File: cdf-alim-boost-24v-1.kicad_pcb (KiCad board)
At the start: 4 copper layers, 89 parts, among them J1 Conn_01x02, J2 Conn_01x02, J3 Conn_01x02, Q1 BSC019N04LS, Q2 BSC019N04LS, Q3 BSC019N04LS, Q4 BSC019N04LS, Q5 BSC019N04LS, U1 HT753-1, U2 TPS25983, U4 LM5122

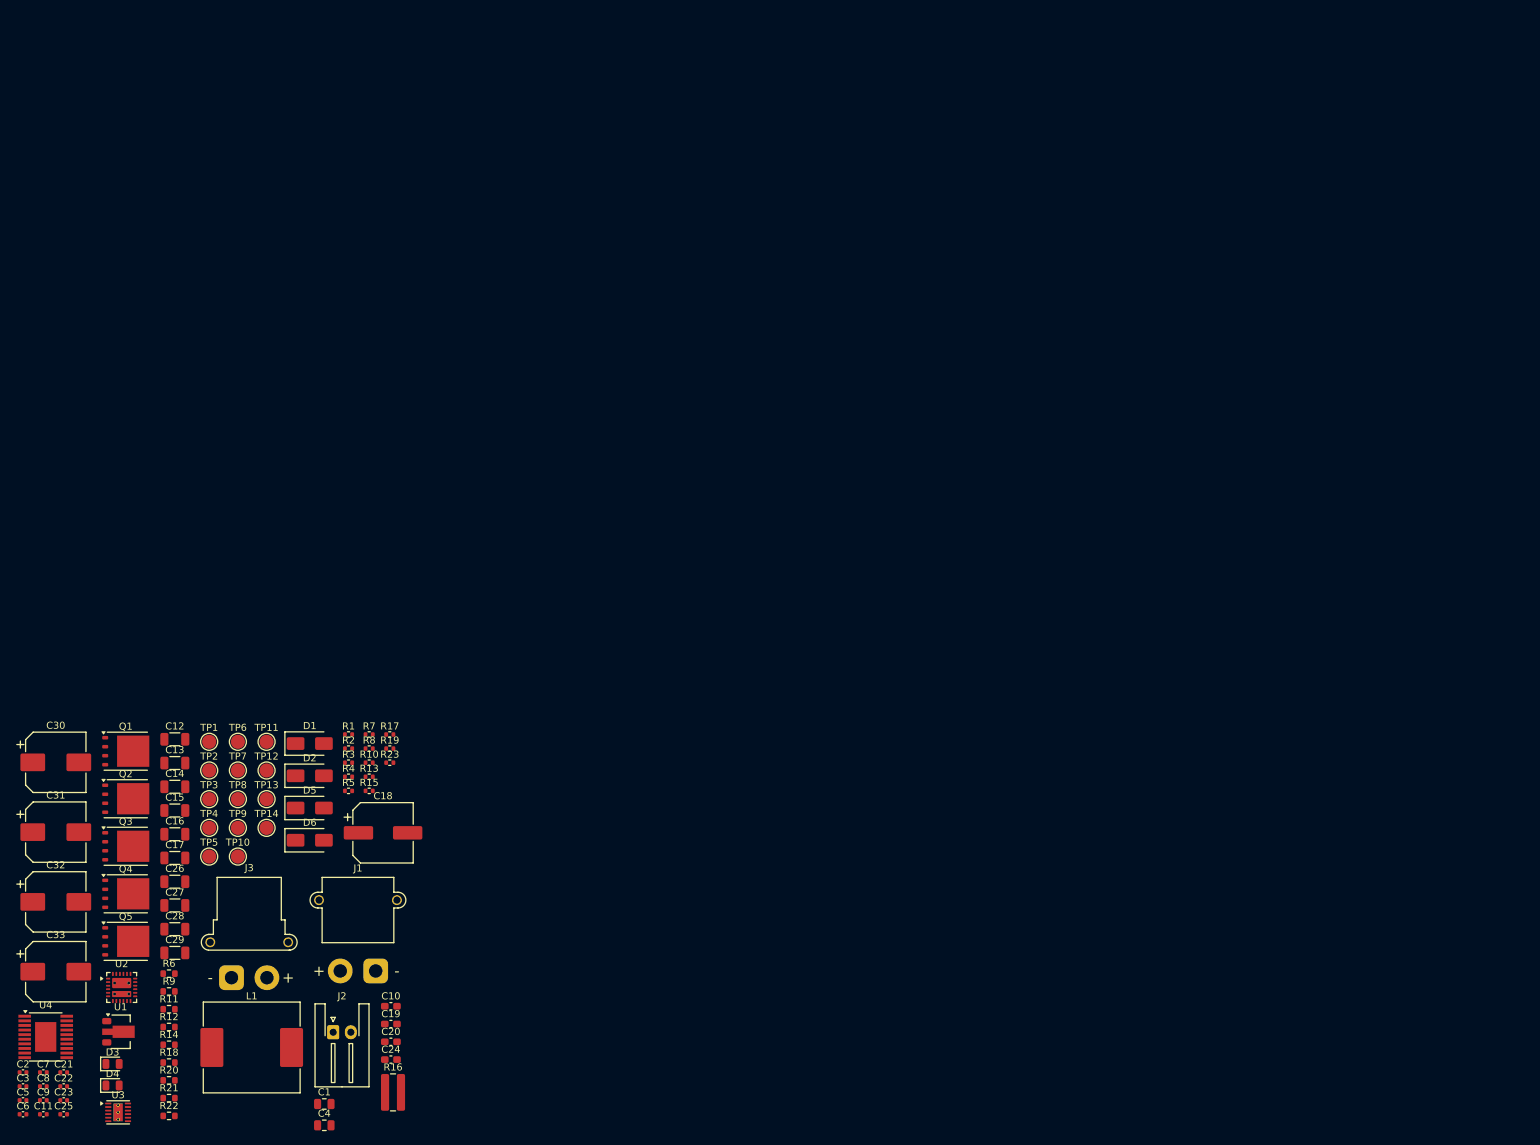
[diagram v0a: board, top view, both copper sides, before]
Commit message: pcb: initial sectionning
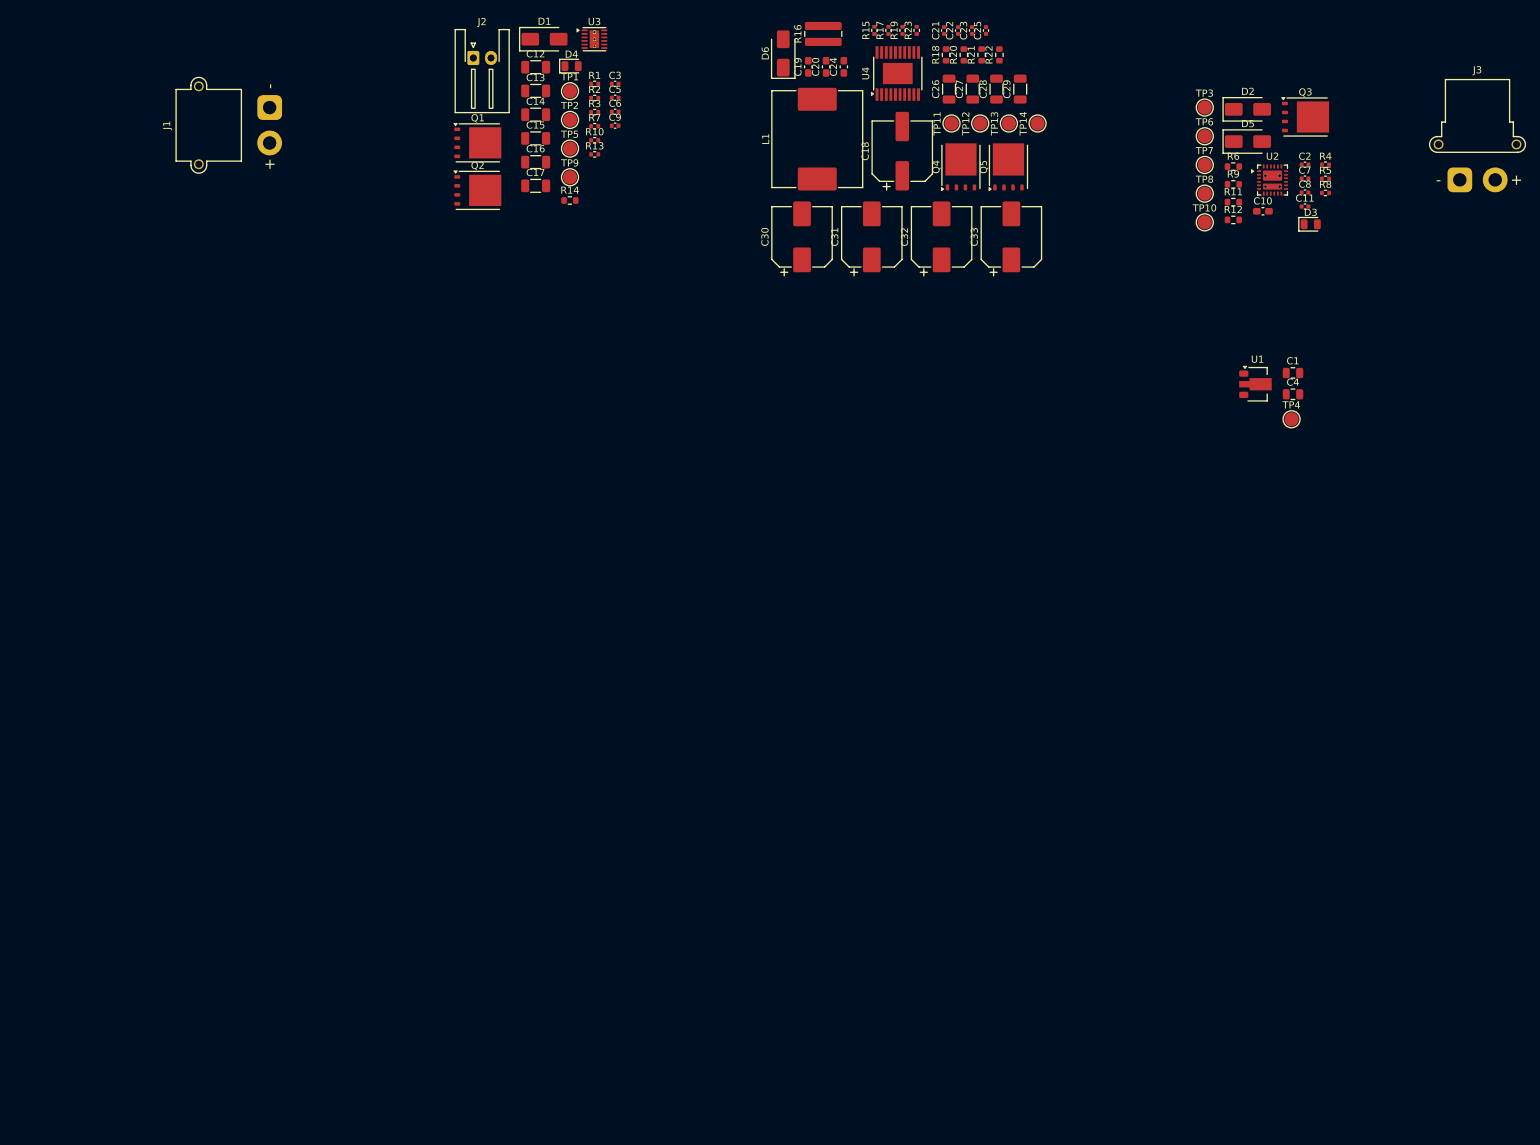
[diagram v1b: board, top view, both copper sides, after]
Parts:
- moved C2 221.7 mm to (199.2, 58.3)
- moved C11 219.4 mm to (199.2, 64.2)
- moved C7 218.3 mm to (199.2, 60.3)
- moved C8 218.3 mm to (199.2, 62.2)
- moved J3 206.8 mm to (221.0, 60.5)
- moved D3 206.5 mm to (200.0, 66.7)
- moved C25 200.9 mm to (154.1, 39.4), turned to 90 degrees
- moved U2 198.4 mm to (194.6, 60.5)
- moved C23 198.1 mm to (152.2, 39.4), turned to 90 degrees
- moved Q3 195.8 mm to (199.2, 51.6)
- moved C22 195.3 mm to (150.2, 39.4), turned to 90 degrees
- moved C21 192.6 mm to (148.2, 39.4), turned to 90 degrees
- moved R22 190.2 mm to (156.0, 42.8), turned to 90 degrees
- moved R11 188.5 mm to (189.0, 63.6)
- moved R12 188.5 mm to (189.0, 66.1)
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
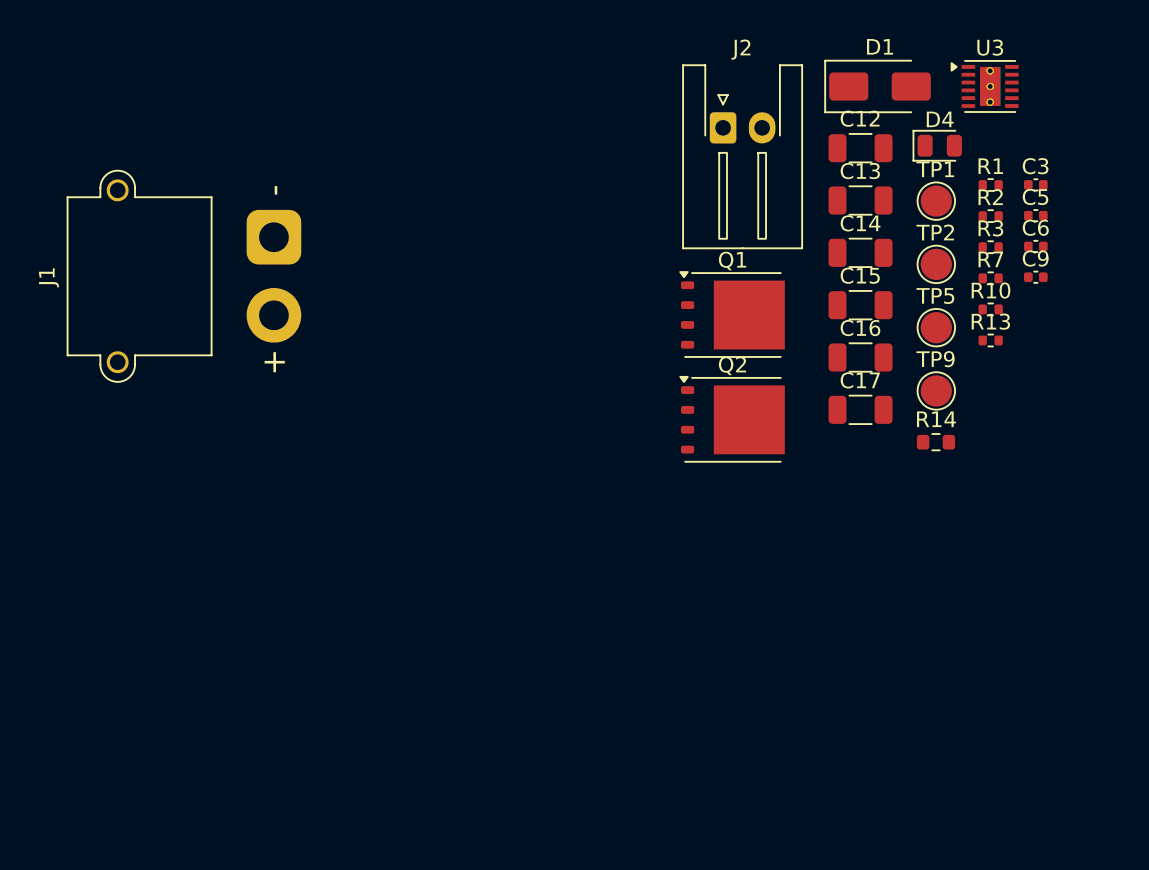
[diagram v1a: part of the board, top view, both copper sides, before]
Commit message: pcb: add lm7480 layout
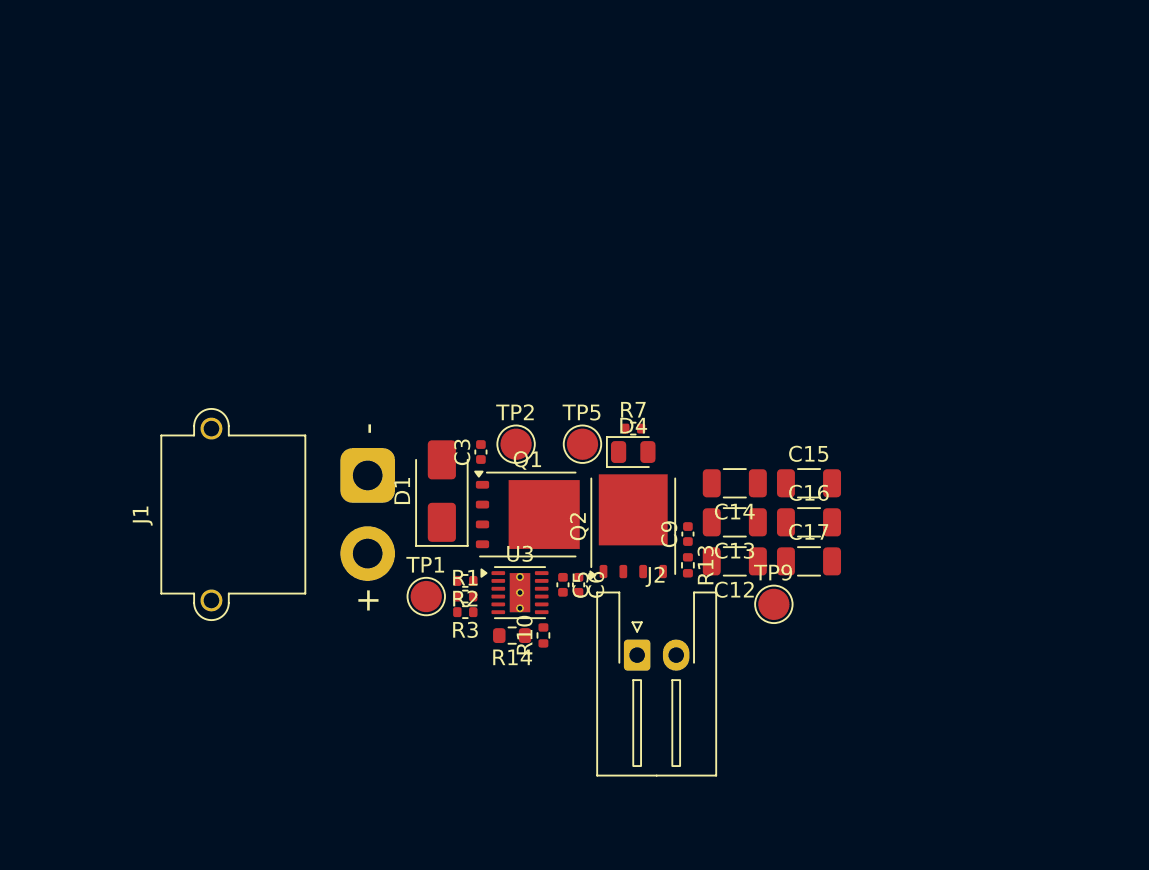
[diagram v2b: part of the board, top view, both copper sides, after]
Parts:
- moved U3 44.2 mm to (68.8, 73.0)
- moved R1 42.7 mm to (65.2, 73.2)
- moved TP1 41.3 mm to (62.8, 73.2)
- moved R3 40.9 mm to (65.2, 74.2), turned to 180 degrees
- moved R2 40.9 mm to (65.2, 72.2), turned to 180 degrees
- moved C3 39.4 mm to (66.2, 64.0), turned to 90 degrees
- moved C5 38.4 mm to (71.5, 72.5), turned to -90 degrees
- moved D1 38.2 mm to (63.8, 66.5), turned to 90 degrees
- moved C6 36.4 mm to (72.5, 72.5), turned to -90 degrees
- moved R10 35.4 mm to (70.2, 75.7), turned to 90 degrees
- moved J2 34.2 mm to (76.2, 77.0)
- moved R14 29.8 mm to (68.2, 75.8), turned to 180 degrees
- moved TP2 29.3 mm to (68.5, 63.5)
- moved D4 27.7 mm to (76.0, 64.0)
- moved C9 27.7 mm to (79.5, 69.2), turned to 90 degrees
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
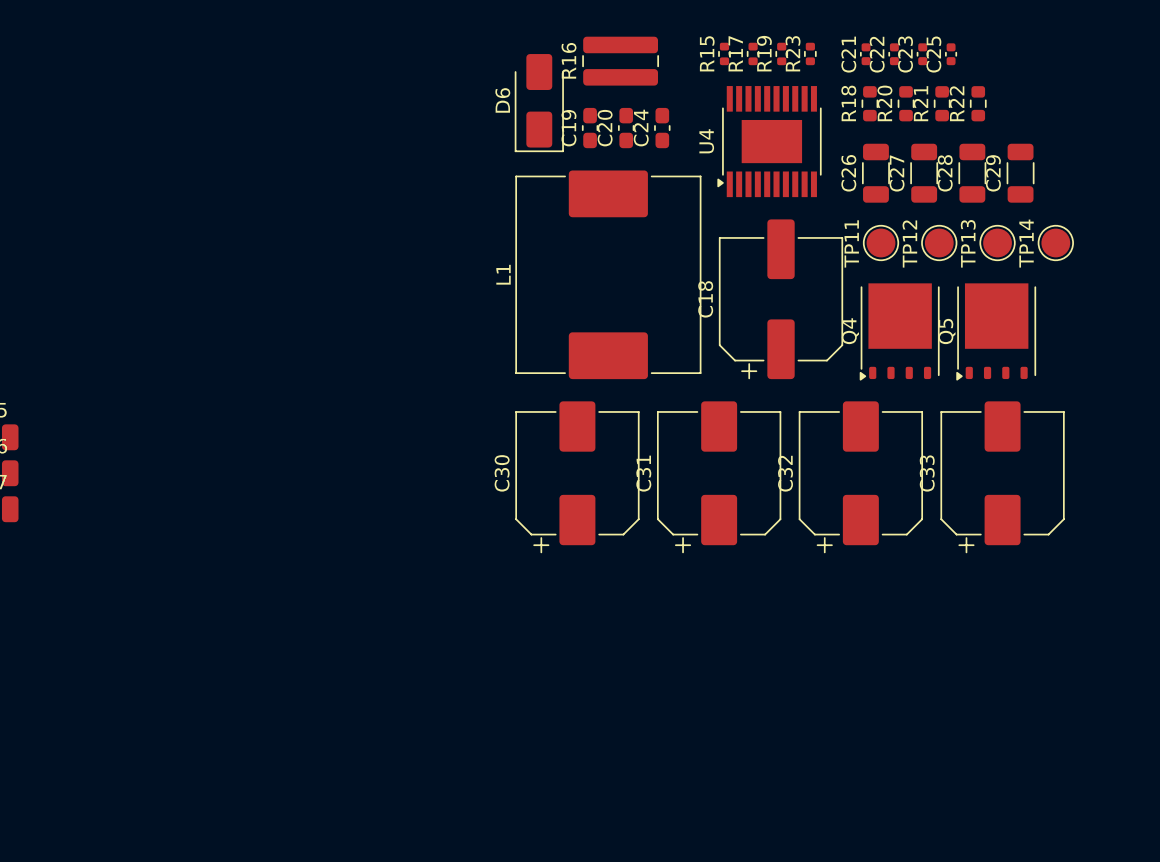
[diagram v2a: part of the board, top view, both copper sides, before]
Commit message: pcb: add boost layout
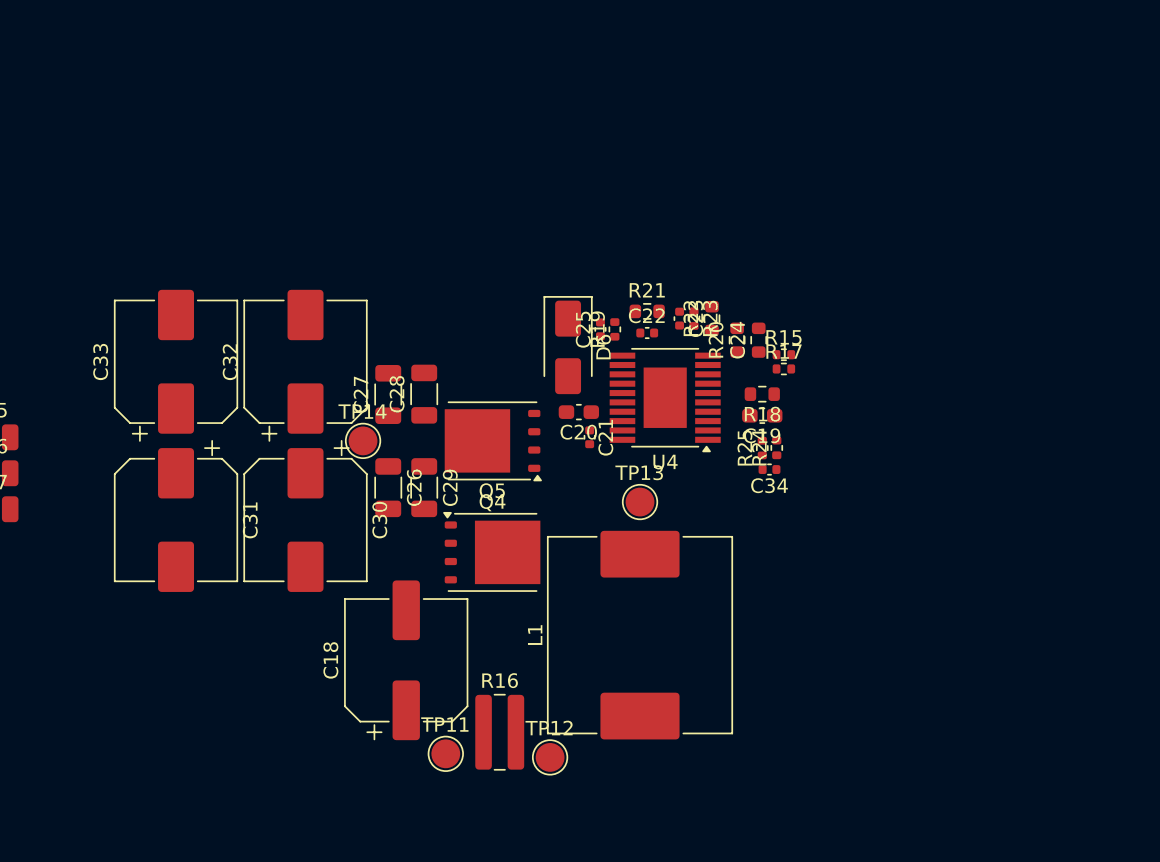
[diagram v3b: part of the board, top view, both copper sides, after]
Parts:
- added C34: 0n1, Capacitor_SMD:C_0402_1005Metric, F.Cu at (141.5, 68.2)
- added R24: 100, Resistor_SMD:R_0402_1005Metric, F.Cu at (142.0, 66.7)
- added R25: 100, Resistor_SMD:R_0402_1005Metric, F.Cu at (141.0, 66.8)
- C24: footprint Capacitor_SMD:C_0603_1608Metric_Pad1.08x0.95mm_HandSolder -> Resistor_SMD:R_0603_1608Metric
- moved C33 58.0 mm to (100.2, 60.8)
- moved TP14 50.1 mm to (113.2, 66.2), turned to 0 degrees
- moved R16 47.4 mm to (122.8, 86.5), turned to 0 degrees
- moved C29 46.9 mm to (117.5, 69.5), turned to -90 degrees
- moved TP11 46.6 mm to (119.0, 88.0), turned to 0 degrees
- moved TP12 44.8 mm to (126.2, 88.2), turned to 0 degrees
- moved C28 41.1 mm to (117.5, 63.0)
- moved C26 40.3 mm to (115.0, 69.5), turned to -90 degrees
- moved C27 40.3 mm to (115.0, 63.0)
- moved C32 39.4 mm to (109.2, 60.8)
- moved C31 37.9 mm to (100.2, 71.8), turned to -90 degrees
- moved C18 36.2 mm to (116.2, 81.5)
- moved Q5 35.9 mm to (122.2, 66.2), turned to 180 degrees
- moved C21 32.8 mm to (129.0, 66.0), turned to -90 degrees
- moved Q4 32.2 mm to (122.2, 74.0), turned to 0 degrees
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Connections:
- L1 pad 1: Net-(U4-CSN) -> Net-(L1-Pad1)
- R16 pad 2: Net-(U4-CSN) -> Net-(L1-Pad1)
- TP12 pad 1: Net-(U4-CSN) -> Net-(L1-Pad1)
- U4 pad 4: +18V -> Net-(U4-CSP)
